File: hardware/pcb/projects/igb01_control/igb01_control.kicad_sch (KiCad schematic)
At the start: 435 parts, among them J1 CODEC_LEFT, J10 ST_JACK_IGB_OUT, J13 Micro_SD_Card, J14 ST_JACK_IGB_IN, J15 ST_JACK_MIDI_OUT, J16 ST_JACK_MIDI_IN, J17 JACK_RST_OUT, J18 JACK_CV1_IN, J19 JACK_CV2_IN, J2 CODEC_RIGHT, J20 JACK_CV1_OUT, J21 JACK_CV2_OUT, J22 JACK_CV3_OUT, J23 JACK_CV4_OUT, J24 JACK_SND_L_OUT, J25 JACK_SND_R_OUT, J26 JACK_RTN_L_IN, J27 JACK_RTN_R_IN, J28 JACK_MAIN_L_OUT, J29 JACK_MAIN_R_OUT, J3 LEFT_CON, J30 JACK_EXT_L_IN, J31 JACK_EXT_R_IN, J32 Hold_Conn, J33 Hold_Conn, J34 ST_JACK_PHONE_OUT, J35 TYPE_SELECT, J36 TYPE_SELECT, J37 Hold_Conn, J38 Hold_Conn, J39 Hold_Conn, J4 RIGHT_CON, J40 Hold_Conn, J41 USB_CONN, J5 POWER_CON, J6 LedDrvConn, J7 McuConn, J8 SWD_CON, J9 JACK_CLK_OUT, Q1 MMBT3904, Q2 MMBT3904, Q3 MMBT3904, Q4 MMBT3904, Q5 MMBT3904, Q6 MMBT3904, Q7 MMBT3904, Q8 MMBT3904, SW59 SW_Push, SW60 SW_Push, SW61 SW_Push, SW62 SW_Push, SW63 SW_Push, SW64 SW_Push, SW65 SW_Push, SW66 SW_Push, SW67 SW_Push, SW68 SW_Push, SW69 SW_Push, SW70 SW_Push, SW71 SW_Push, SW72 SW_Push, SW73 SW_Push, SW74 SW_Push, SW75 SW_Push, SW76 SW_Push, U1 R-78B5.0-2.0, U10 LDK320M18R, U11 MCP6001, U12 74AHCT1G125, U13 TLP2361, U14 TL074, U15 TL074, U16 DAC8165, U17 TL074, U18 TL074, U19 MCP6002, U2 SSP7603P33PR, U20 LM4040DBZ-5, U21 OPA2156, U3 STM32G431RBTx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

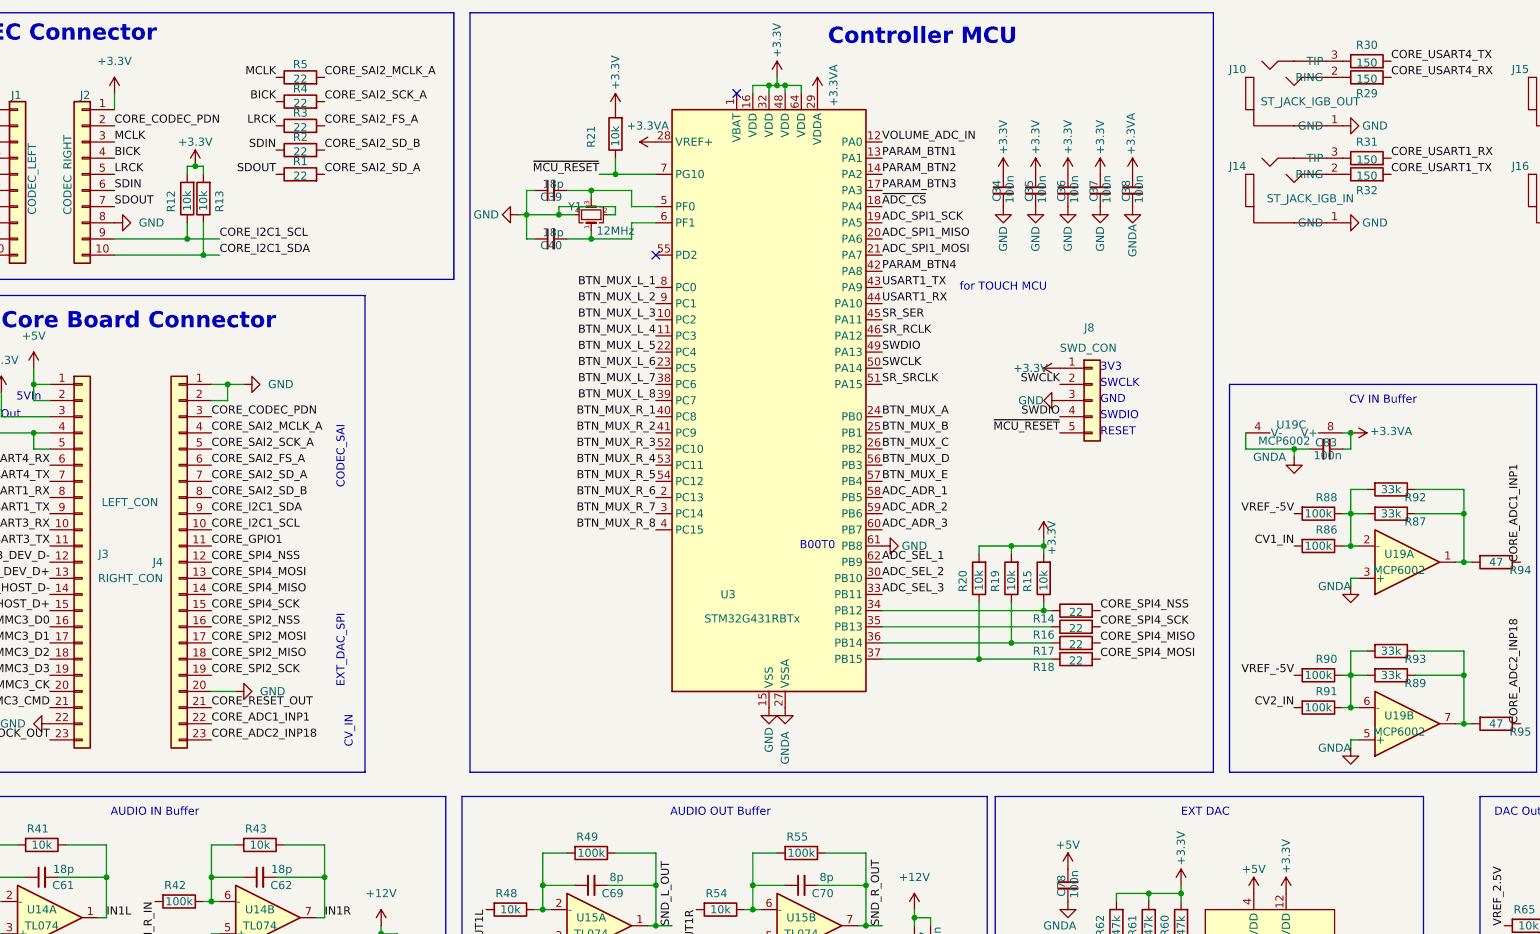
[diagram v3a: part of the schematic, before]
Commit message: update igb01 module control board
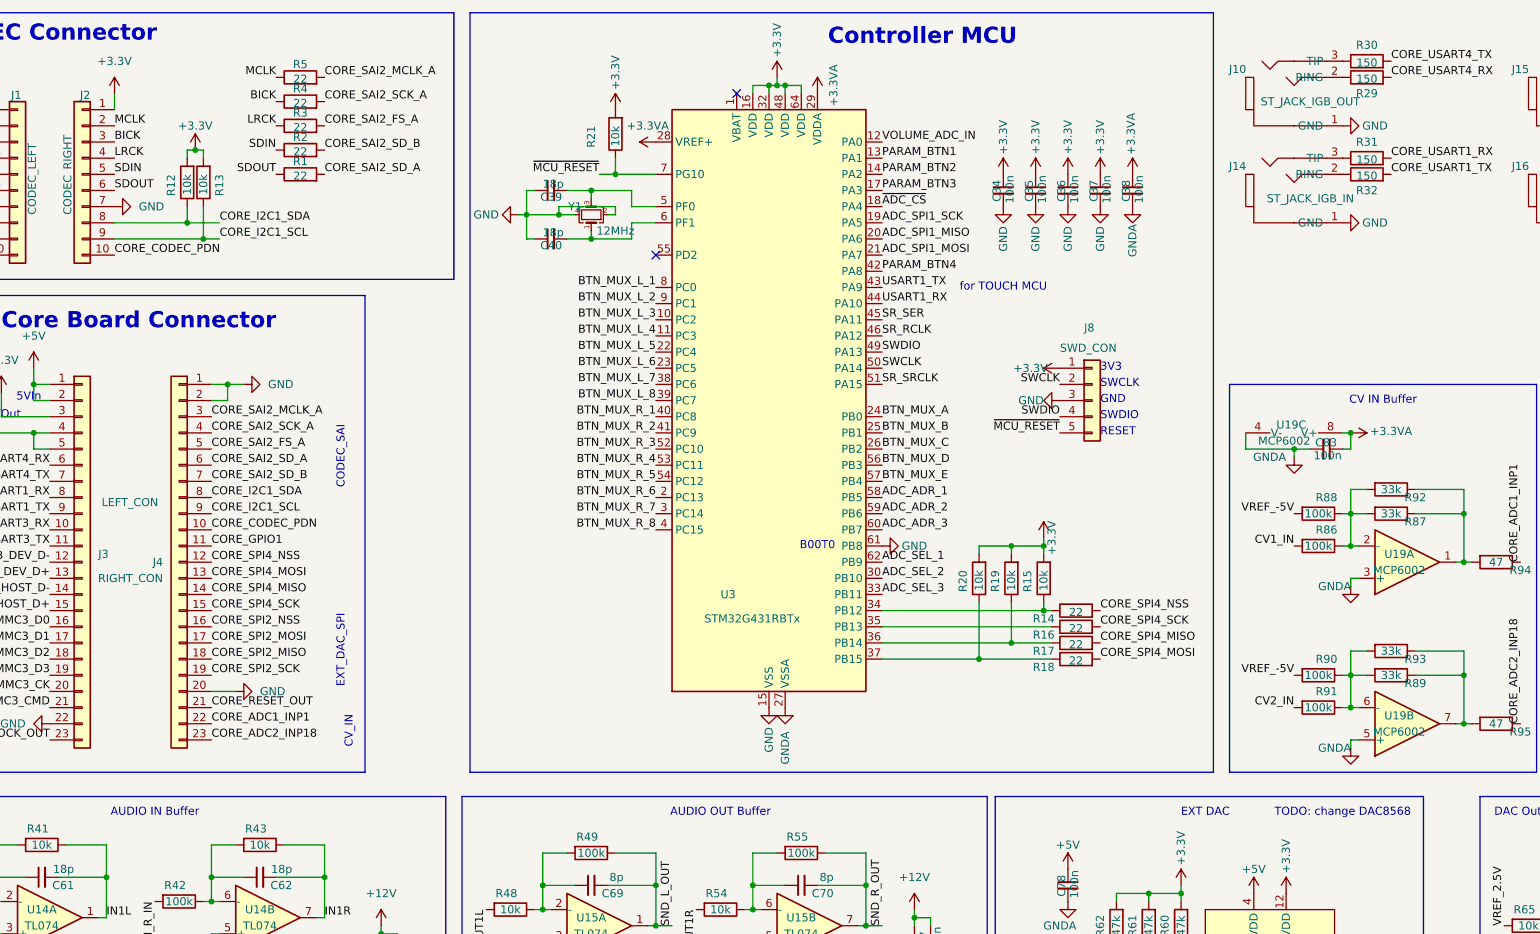
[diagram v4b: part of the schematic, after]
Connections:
- net BICK: now also J2.3 (Pin_3); no longer J2.4 (Pin_4)
- net CORE_CODEC_PDN: now also J2.10 (Pin_10), J4.10 (Pin_10); no longer J2.2 (Pin_2), J4.3 (Pin_3)
- net CORE_I2C1_SCL: now also J4.9 (Pin_9), R13.1; no longer J4.10 (Pin_10), R12.1
- net CORE_I2C1_SDA: now also J2.8 (Pin_8), J4.8 (Pin_8), R12.1; no longer J2.10 (Pin_10), J4.9 (Pin_9), R13.1
- net CORE_SAI2_FS_A: now also J4.5 (Pin_5); no longer J4.6 (Pin_6)
- net CORE_SAI2_MCLK_A: now also J4.3 (Pin_3); no longer J4.4 (Pin_4)
- net CORE_SAI2_SCK_A: now also J4.4 (Pin_4); no longer J4.5 (Pin_5)
- net CORE_SAI2_SD_A: now also J4.6 (Pin_6); no longer J4.7 (Pin_7)
- net CORE_SAI2_SD_B: now also J4.7 (Pin_7); no longer J4.8 (Pin_8)
- net GND: now also J2.7 (Pin_7); no longer J2.8 (Pin_8)
- net LRCK: now also J2.4 (Pin_4); no longer J2.5 (Pin_5)
- net MCLK: now also J2.2 (Pin_2); no longer J2.3 (Pin_3)
- net SDIN: now also J2.5 (Pin_5); no longer J2.6 (Pin_6)
- net SDOUT: now also J2.6 (Pin_6); no longer J2.7 (Pin_7)
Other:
- note added: "TODO: change DAC8568"
- moved on the sheet: R12, R13
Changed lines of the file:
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@@
 		)
 	)
+	(text "TODO: change DAC8568"
+		(exclude_from_sim no)
+		(at 240.03 140.97 0)
+		(effects
+			(font
+				(size 1.27 1.27)
+			)
+		)
+	)
 	(text "Volume"
 		(exclude_from_sim no)
@@
 	)
 	(junction
-		(at 58.42 50.8)
+		(at 58.42 48.26)
 		(diameter 0)
 		(color 0 0 0 0)
@@
 	)
 	(junction
-		(at 59.69 39.37)
+		(at 59.69 36.83)
 		(diameter 0)
 		(color 0 0 0 0)
@@
 	)
 	(junction
-		(at 60.96 53.34)
+		(at 60.96 50.8)
 		(diameter 0)
 		(color 0 0 0 0)
@@
 	(wire
 		(pts
-			(xy 58.42 50.8) (xy 63.5 50.8)
+			(xy 58.42 48.26) (xy 63.5 48.26)
 		)
 		(stroke
@@
 	(wire
 		(pts
-			(xy 58.42 50.8) (xy 46.99 50.8)
+			(xy 58.42 48.26) (xy 46.99 48.26)
 		)
 		(stroke
@@
 	(wire
 		(pts
-			(xy 58.42 39.37) (xy 58.42 40.64)
+			(xy 58.42 36.83) (xy 58.42 38.1)
 		)
 		(stroke
@@
 	(wire
 		(pts
-			(xy 58.42 48.26) (xy 58.42 50.8)
+			(xy 58.42 45.72) (xy 58.42 48.26)
 		)
 		(stroke
@@
 	(wire
 		(pts
-			(xy 46.99 53.34) (xy 60.96 53.34)
+			(xy 46.99 50.8) (xy 60.96 50.8)
 		)
 		(stroke
@@
 	(wire
 		(pts
-			(xy 60.96 39.37) (xy 60.96 40.64)
+			(xy 60.96 36.83) (xy 60.96 38.1)
 		)
 		(stroke
@@
 	(wire
 		(pts
-			(xy 60.96 48.26) (xy 60.96 53.34)
+			(xy 60.96 45.72) (xy 60.96 50.8)
 		)
 		(stroke
@@
 	(wire
 		(pts
-			(xy 59.69 39.37) (xy 58.42 39.37)
+			(xy 59.69 36.83) (xy 58.42 36.83)
 		)
 		(stroke
@@
 	(wire
 		(pts
-			(xy 60.96 53.34) (xy 63.5 53.34)
+			(xy 60.96 50.8) (xy 63.5 50.8)
 		)
 		(stroke
@@
 	(wire
 		(pts
-			(xy 59.69 39.37) (xy 60.96 39.37)
+			(xy 59.69 36.83) (xy 60.96 36.83)
 		)
 		(stroke
@@
 	)
 	(label "CORE_SAI2_MCLK_A"
-		(at 62.23 81.28 0)
+		(at 62.23 78.74 0)
 		(effects
 			(font
@@
 	)
 	(label "CORE_SAI2_SD_B"
-		(at 62.23 91.44 0)
+		(at 62.23 88.9 0)
 		(effects
 			(font
@@
 	)
 	(label "SDOUT"
-		(at 46.99 45.72 0)
+		(at 46.99 43.18 0)
 		(effects
 			(font
@@
 	)
 	(label "BICK"
-		(at 46.99 38.1 0)
+		(at 46.99 35.56 0)
 		(effects
 			(font
@@
 	)
 	(label "CORE_SAI2_SCK_A"
-		(at 62.23 83.82 0)
+		(at 62.23 81.28 0)
 		(effects
 			(font
@@
 	)
 	(label "CORE_I2C1_SDA"
-		(at 63.5 53.34 0)
+		(at 63.5 48.26 0)
 		(effects
 			(font
@@
 	)
 	(label "CORE_I2C1_SDA"
-		(at 62.23 93.98 0)
+		(at 62.23 91.44 0)
 		(effects
 			(font
@@
 	)
 	(label "MCLK"
-		(at 46.99 35.56 0)
+		(at 46.99 33.02 0)
 		(effects
 			(font
@@
 	)
 	(label "LRCK"
-		(at 46.99 40.64 0)
+		(at 46.99 38.1 0)
 		(effects
 			(font
@@
 	)
 	(label "CORE_SAI2_SD_A"
-		(at 62.23 88.9 0)
+		(at 62.23 86.36 0)
 		(effects
 			(font
@@
 	)
 	(label "CORE_I2C1_SCL"
-		(at 62.23 96.52 0)
+		(at 62.23 93.98 0)
 		(effects
 			(font
@@
 	)
 	(label "CORE_CODEC_PDN"
-		(at 46.99 33.02 0)
+		(at 46.99 53.34 0)
 		(effects
 			(font
@@
 	)
 	(label "SDIN"
-		(at 46.99 43.18 0)
+		(at 46.99 40.64 0)
 		(effects
 			(font
@@
 	)
 	(label "CORE_SAI2_FS_A"
-		(at 62.23 86.36 0)
+		(at 62.23 83.82 0)
 		(effects
 			(font
@@
 	)
 	(label "CORE_CODEC_PDN"
-		(at 62.23 78.74 0)
+		(at 62.23 96.52 0)
 		(effects
 			(font
@@
 	(symbol
 		(lib_id "C_Quencer2-led-rescue:R-cqd_touch_pad")
-		(at 60.96 44.45 180)
+		(at 60.96 41.91 180)
 		(unit 1)
 		(exclude_from_sim no)
@@
 		(dnp no)
 		(property "Reference" "R13"
-			(at 63.5 43.18 90)
+			(at 63.5 40.64 90)
 			(effects
 				(font
@@
 		)
 		(property "Value" "10k"
-			(at 60.96 43.18 90)
+			(at 60.96 40.64 90)
 			(effects
 				(font
@@
 		)
 		(property "Footprint" "Resistor_SMD:R_0603_1608Metric"
-			(at 62.738 44.45 90)
+			(at 62.738 41.91 90)
 			(effects
 				(font
@@
 		)
 		(property "Datasheet" ""
-			(at 60.96 44.45 0)
+			(at 60.96 41.91 0)
 			(effects
 				(font
@@
 		)
 		(property "Description" ""
-			(at 60.96 44.45 0)
+			(at 60.96 41.91 0)
 			(effects
 				(font
@@
 	(symbol
 		(lib_id "C_Quencer2-led-rescue:R-cqd_touch_pad")
-		(at 58.42 44.45 180)
+		(at 58.42 41.91 180)
 		(unit 1)
 		(exclude_from_sim no)
@@
 		(dnp no)
 		(property "Reference" "R12"
-			(at 55.88 43.18 90)
+			(at 55.88 40.64 90)
 			(effects
 				(font
@@
 		)
 		(property "Value" "10k"
-			(at 58.42 43.18 90)
+			(at 58.42 40.64 90)
 			(effects
 				(font
@@
 		)
 		(property "Footprint" "Resistor_SMD:R_0603_1608Metric"
-			(at 60.198 44.45 90)
+			(at 60.198 41.91 90)
 			(effects
 				(font
@@
 		)
 		(property "Datasheet" ""
-			(at 58.42 44.45 0)
+			(at 58.42 41.91 0)
 			(effects
 				(font
@@
 		)
 		(property "Description" ""
-			(at 58.42 44.45 0)
+			(at 58.42 41.91 0)
 			(effects
 				(font
@@
 	(symbol
 		(lib_id "power:+3.3V")
-		(at 59.69 39.37 0)
+		(at 59.69 36.83 0)
 		(unit 1)
 		(exclude_from_sim no)
@@
 		(dnp no)
 		(property "Reference" "#PWR092"
-			(at 59.69 43.18 0)
+			(at 59.69 40.64 0)
 			(effects
 				(font
@@
 		)
 		(property "Value" "+3.3V"
-			(at 59.69 35.56 0)
+			(at 59.69 33.02 0)
 			(effects
 				(font
@@
 		)
 		(property "Footprint" ""
-			(at 59.69 39.37 0)
+			(at 59.69 36.83 0)
 			(effects
 				(font
@@
 		)
 		(property "Datasheet" ""
-			(at 59.69 39.37 0)
+			(at 59.69 36.83 0)
 			(effects
 				(font
@@
 		)
 		(property "Description" "Power symbol creates a global label with name \"+3.3V\""
-			(at 59.69 39.37 0)
+			(at 59.69 36.83 0)
 			(effects
 				(font
@@
 	(symbol
 		(lib_id "power:GND")
-		(at 46.99 48.26 90)
+		(at 46.99 45.72 90)
 		(unit 1)
 		(exclude_from_sim no)
@@
 		(fields_autoplaced yes)
 		(property "Reference" "#PWR03"
-			(at 53.34 48.26 0)
+			(at 53.34 45.72 0)
 			(effects
 				(font
@@
 		)
 		(property "Value" "GND"
-			(at 50.8 48.2599 90)
+			(at 50.8 45.7199 90)
 			(effects
 				(font
@@
 		)
 		(property "Footprint" ""
-			(at 46.99 48.26 0)
+			(at 46.99 45.72 0)
 			(effects
 				(font
@@
 		)
 		(property "Datasheet" ""
-			(at 46.99 48.26 0)
+			(at 46.99 45.72 0)
 			(effects
 				(font
@@
 		)
 		(property "Description" "Power symbol creates a global label with name \"GND\" , ground"
-			(at 46.99 48.26 0)
+			(at 46.99 45.72 0)
 			(effects
 				(font
